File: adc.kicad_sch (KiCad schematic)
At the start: 15 parts, among them U16001 ADS8665IPWR

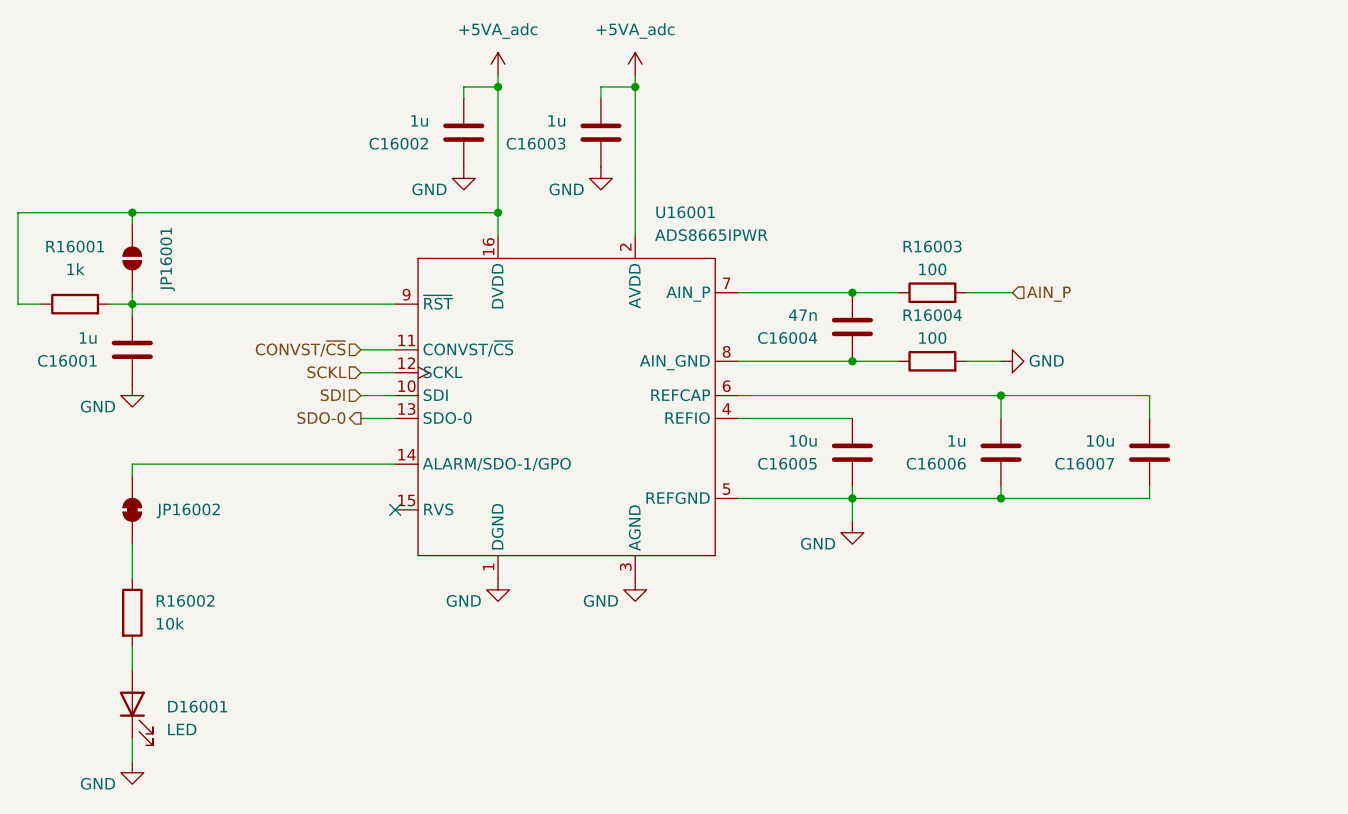
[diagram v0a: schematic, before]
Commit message: add pss 3dmodels and testpoints
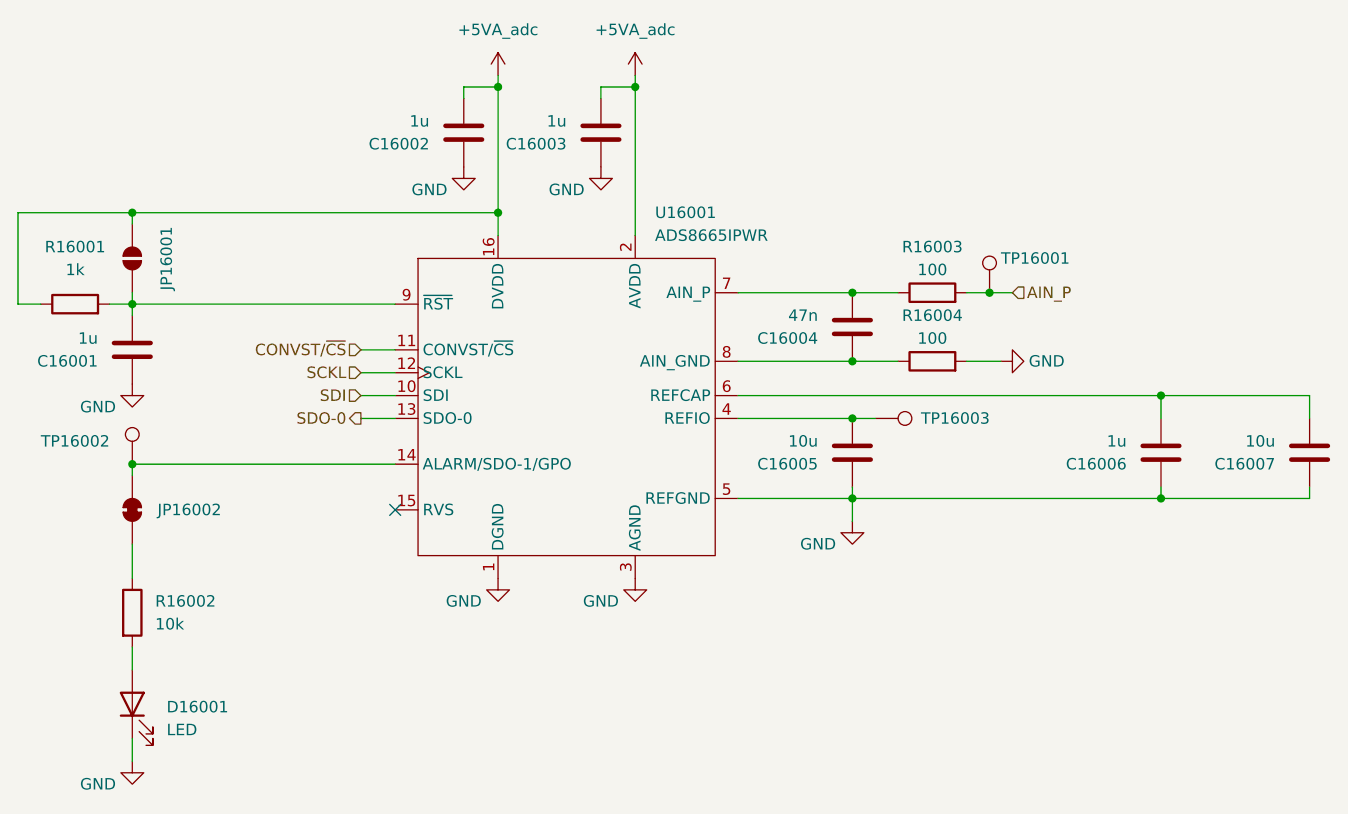
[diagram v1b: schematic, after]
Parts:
- added TP16001, TP16002, TP16003: ~, pss:TP_0805_2012Metric, symbol Connector:TestPoint
- JP16001: footprint (none) -> Jumper:SolderJumper-2_P1.3mm_Open_RoundedPad1.0x1.5mm
- JP16002: footprint (none) -> pss:SolderJumper-2_P1.3mm_Bridged-Soldermask-Paste_RoundedPad1.0x1.5mm
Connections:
- net AIN_P: now also TP16001.1
- net at C16005.2, U16001.4 (REFIO): now also TP16003.1
- net at JP16002.2 (B), U16001.14 (ALARM/SDO-1/GPO): now also TP16002.1
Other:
- moved on the sheet: C16006, C16007

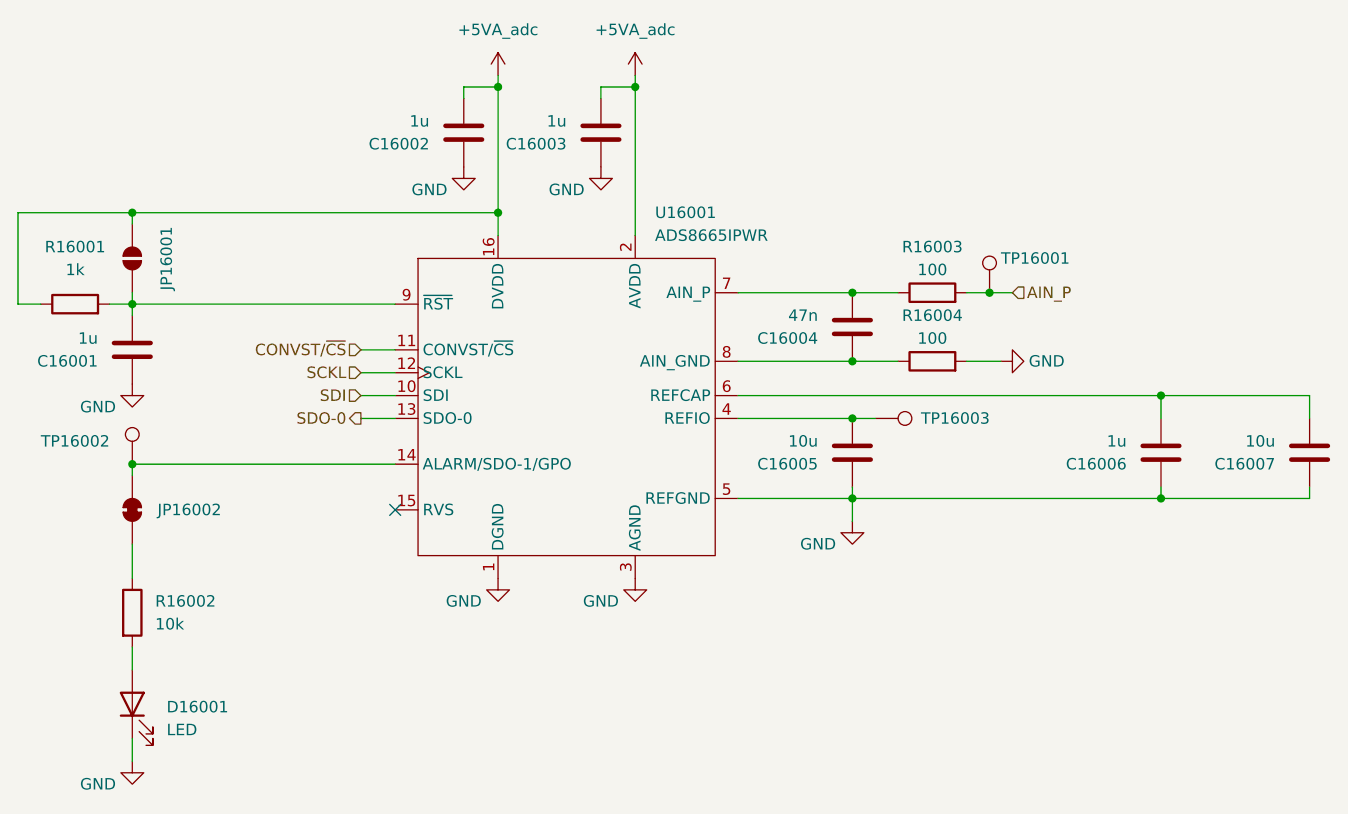
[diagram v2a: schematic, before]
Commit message: edit pss reannotate entire schematic
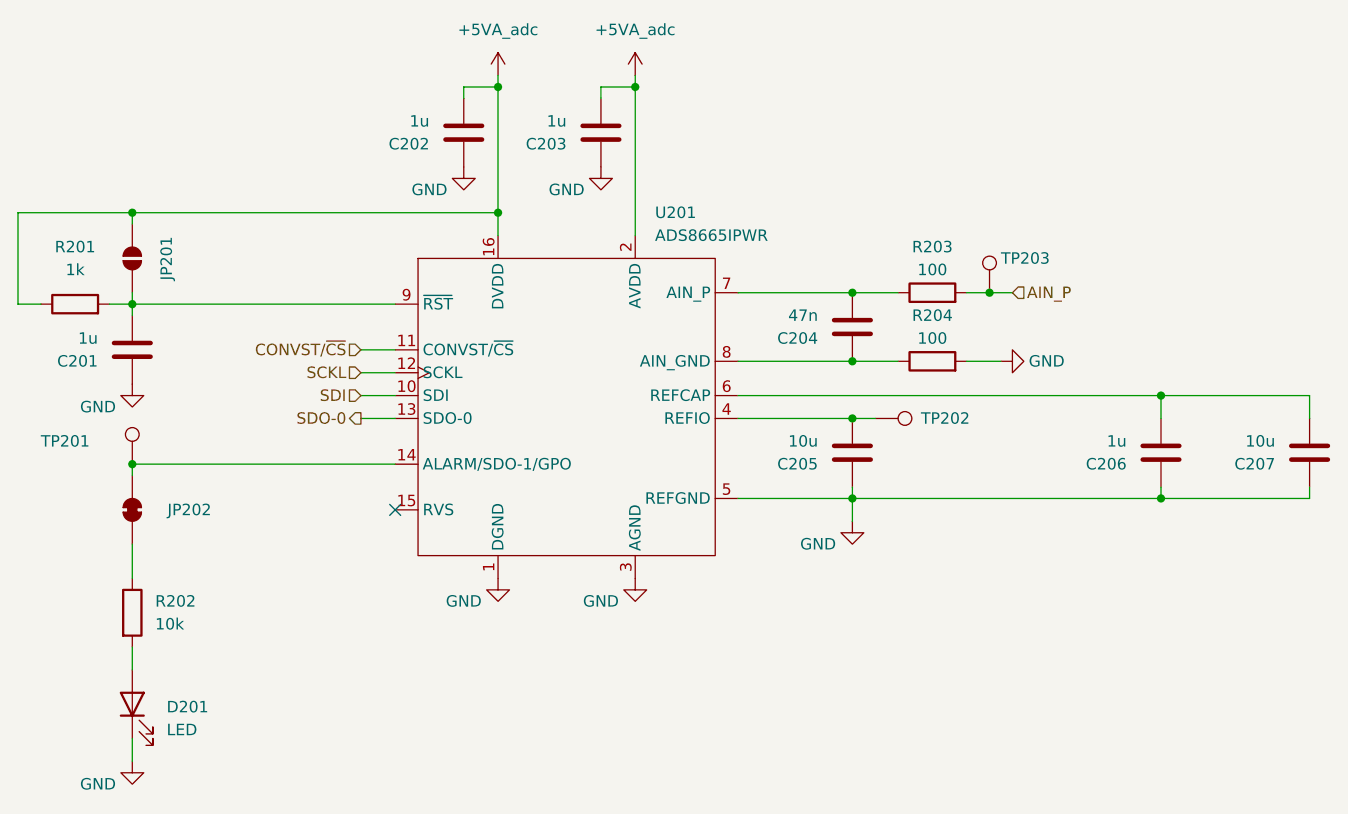
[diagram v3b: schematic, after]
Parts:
- renumbered C16001 to C201, C16002 to C202, C16003 to C203, C16004 to C204, C16005 to C205, C16006 to C206, C16007 to C207, D16001 to D201, JP16001 to JP201, JP16002 to JP202, R16001 to R201, R16002 to R202, R16003 to R203, R16004 to R204, TP16002 to TP201, TP16003 to TP202, TP16001 to TP203, U16001 to U201

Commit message: edit pss symbol library: export all schematic symbols to library 'pss' and update symbol link
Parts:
- D201: symbol Device:LED -> pss:LED
- JP201: symbol Jumper:SolderJumper_2_Open -> pss:SolderJumper_2_Open
- JP202: symbol Jumper:SolderJumper_2_Bridged -> pss:SolderJumper_2_Bridged
- TP201, TP202, TP203: symbol Connector:TestPoint -> pss:TestPoint
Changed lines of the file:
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@@
 	)
 	(symbol
-		(lib_id "Connector:TestPoint")
+		(lib_id "pss:TestPoint")
 		(at 171.45 99.06 270)
 		(unit 1)
@@
 	)
 	(symbol
-		(lib_id "Connector:TestPoint")
+		(lib_id "pss:TestPoint")
 		(at 184.15 85.09 0)
 		(unit 1)
@@
 	)
 	(symbol
-		(lib_id "Connector:TestPoint")
+		(lib_id "pss:TestPoint")
 		(at 88.9 104.14 0)
 		(unit 1)
@@
 	)
 	(symbol
-		(lib_id "Jumper:SolderJumper_2_Open")
+		(lib_id "pss:SolderJumper_2_Open")
 		(at 88.9 81.28 270)
 		(unit 1)
@@
 	)
 	(symbol
-		(lib_id "Device:LED")
+		(lib_id "pss:LED")
 		(at 88.9 130.81 90)
 		(unit 1)
@@
 	)
 	(symbol
-		(lib_id "Jumper:SolderJumper_2_Bridged")
+		(lib_id "pss:SolderJumper_2_Bridged")
 		(at 88.9 109.22 90)
 		(unit 1)

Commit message: edit pss footprint library: export all footprints to library 'pss' and update footprint links
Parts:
- C201, C202, C203, C206: footprint Capacitor_SMD:C_0603_1608Metric_Pad1.08x0.95mm_HandSolder -> pss:C_0603_1608Metric_Pad1.08x0.95mm_HandSolder
- C204: footprint Capacitor_SMD:C_1206_3216Metric_Pad1.33x1.80mm_HandSolder -> pss:C_1206_3216Metric_Pad1.33x1.80mm_HandSolder
- C205, C207: footprint Capacitor_SMD:C_1210_3225Metric_Pad1.33x2.70mm_HandSolder -> pss:C_1210_3225Metric_Pad1.33x2.70mm_HandSolder
- D201: footprint LED_SMD:LED_0805_2012Metric_Pad1.15x1.40mm_HandSolder -> pss:LED_0805_2012Metric_Pad1.15x1.40mm_HandSolder
- JP201: footprint Jumper:SolderJumper-2_P1.3mm_Open_RoundedPad1.0x1.5mm -> pss:SolderJumper-2_P1.3mm_Open_RoundedPad1.0x1.5mm
- R201, R202, R203, R204: footprint Resistor_SMD:R_1210_3225Metric_Pad1.30x2.65mm_HandSolder -> pss:R_1210_3225Metric_Pad1.30x2.65mm_HandSolder
- U201: footprint Package_SO:TSSOP-16_4.4x5mm_P0.65mm -> pss:TSSOP-16_4.4x5mm_P0.65mm
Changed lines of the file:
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@@
 			)
 		)
-		(property "Footprint" "Capacitor_SMD:C_0603_1608Metric_Pad1.08x0.95mm_HandSolder"
+		(property "Footprint" "pss:C_0603_1608Metric_Pad1.08x0.95mm_HandSolder"
 			(at 87.9348 87.63 0)
 			(effects
@@
 			)
 		)
-		(property "Footprint" "Resistor_SMD:R_1210_3225Metric_Pad1.30x2.65mm_HandSolder"
+		(property "Footprint" "pss:R_1210_3225Metric_Pad1.30x2.65mm_HandSolder"
 			(at 177.8 86.868 90)
 			(effects
@@
 			)
 		)
-		(property "Footprint" "Capacitor_SMD:C_1210_3225Metric_Pad1.33x2.70mm_HandSolder"
+		(property "Footprint" "pss:C_1210_3225Metric_Pad1.33x2.70mm_HandSolder"
 			(at 167.9448 99.06 0)
 			(effects
@@
 			)
 		)
-		(property "Footprint" "Resistor_SMD:R_1210_3225Metric_Pad1.30x2.65mm_HandSolder"
+		(property "Footprint" "pss:R_1210_3225Metric_Pad1.30x2.65mm_HandSolder"
 			(at 87.122 120.65 90)
 			(effects
@@
 			)
 		)
-		(property "Footprint" "Package_SO:TSSOP-16_4.4x5mm_P0.65mm"
+		(property "Footprint" "pss:TSSOP-16_4.4x5mm_P0.65mm"
 			(at 137.16 133.35 0)
 			(effects
@@
 			)
 		)
-		(property "Footprint" "Capacitor_SMD:C_1206_3216Metric_Pad1.33x1.80mm_HandSolder"
+		(property "Footprint" "pss:C_1206_3216Metric_Pad1.33x1.80mm_HandSolder"
 			(at 167.9448 85.09 0)
 			(effects
@@
 			)
 		)
-		(property "Footprint" "Resistor_SMD:R_1210_3225Metric_Pad1.30x2.65mm_HandSolder"
+		(property "Footprint" "pss:R_1210_3225Metric_Pad1.30x2.65mm_HandSolder"
 			(at 177.8 94.488 90)
 			(effects
@@
 			)
 		)
-		(property "Footprint" "Capacitor_SMD:C_0603_1608Metric_Pad1.08x0.95mm_HandSolder"
+		(property "Footprint" "pss:C_0603_1608Metric_Pad1.08x0.95mm_HandSolder"
 			(at 140.0048 63.5 0)
 			(effects
@@
 			)
 		)
-		(property "Footprint" "Resistor_SMD:R_1210_3225Metric_Pad1.30x2.65mm_HandSolder"
+		(property "Footprint" "pss:R_1210_3225Metric_Pad1.30x2.65mm_HandSolder"
 			(at 82.55 88.138 90)
 			(effects
@@
 			)
 		)
-		(property "Footprint" "Jumper:SolderJumper-2_P1.3mm_Open_RoundedPad1.0x1.5mm"
+		(property "Footprint" "pss:SolderJumper-2_P1.3mm_Open_RoundedPad1.0x1.5mm"
 			(at 88.9 81.28 0)
 			(effects
@@
 			)
 		)
-		(property "Footprint" "Capacitor_SMD:C_1210_3225Metric_Pad1.33x2.70mm_HandSolder"
+		(property "Footprint" "pss:C_1210_3225Metric_Pad1.33x2.70mm_HandSolder"
 			(at 218.7448 99.06 0)
 			(effects
@@
 			)
 		)
-		(property "Footprint" "Capacitor_SMD:C_0603_1608Metric_Pad1.08x0.95mm_HandSolder"
+		(property "Footprint" "pss:C_0603_1608Metric_Pad1.08x0.95mm_HandSolder"
 			(at 124.7648 63.5 0)
 			(effects
@@
 			)
 		)
-		(property "Footprint" "Capacitor_SMD:C_0603_1608Metric_Pad1.08x0.95mm_HandSolder"
+		(property "Footprint" "pss:C_0603_1608Metric_Pad1.08x0.95mm_HandSolder"
 			(at 202.2348 99.06 0)
 			(effects
@@
 			)
 		)
-		(property "Footprint" "LED_SMD:LED_0805_2012Metric_Pad1.15x1.40mm_HandSolder"
+		(property "Footprint" "pss:LED_0805_2012Metric_Pad1.15x1.40mm_HandSolder"
 			(at 88.9 130.81 0)
 			(effects
